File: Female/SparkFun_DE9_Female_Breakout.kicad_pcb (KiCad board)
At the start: 2 copper layers, 22.9 x 31.8 mm, 43 parts, among them J2 Conn_01x09, J3 Conn_01x01, J4 Conn_01x01, J5 DB9-Female

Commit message: Updates symbol, footprint, and design with the new renamed parts
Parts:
- removed J5: DB9-Female, DE9_Footprint:DB9_Female
- added J1: DE9-Female, DE9-Footprints:DE9_Female, F.Cu at (120.3, 108.6)
- moved G*** 0.32 mm to (113.6, 96.5)
- moved Ref** 0.32 mm to (113.6, 121.3)

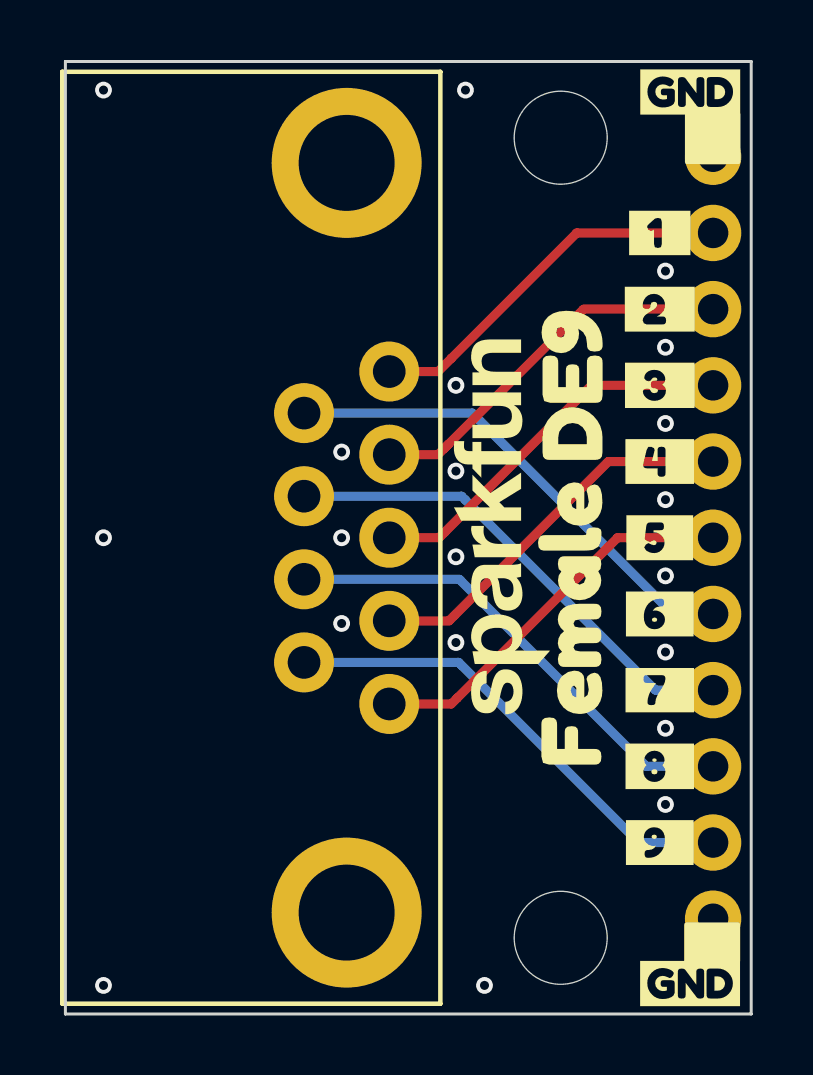
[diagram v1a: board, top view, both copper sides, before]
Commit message: Moves standoff just a bit
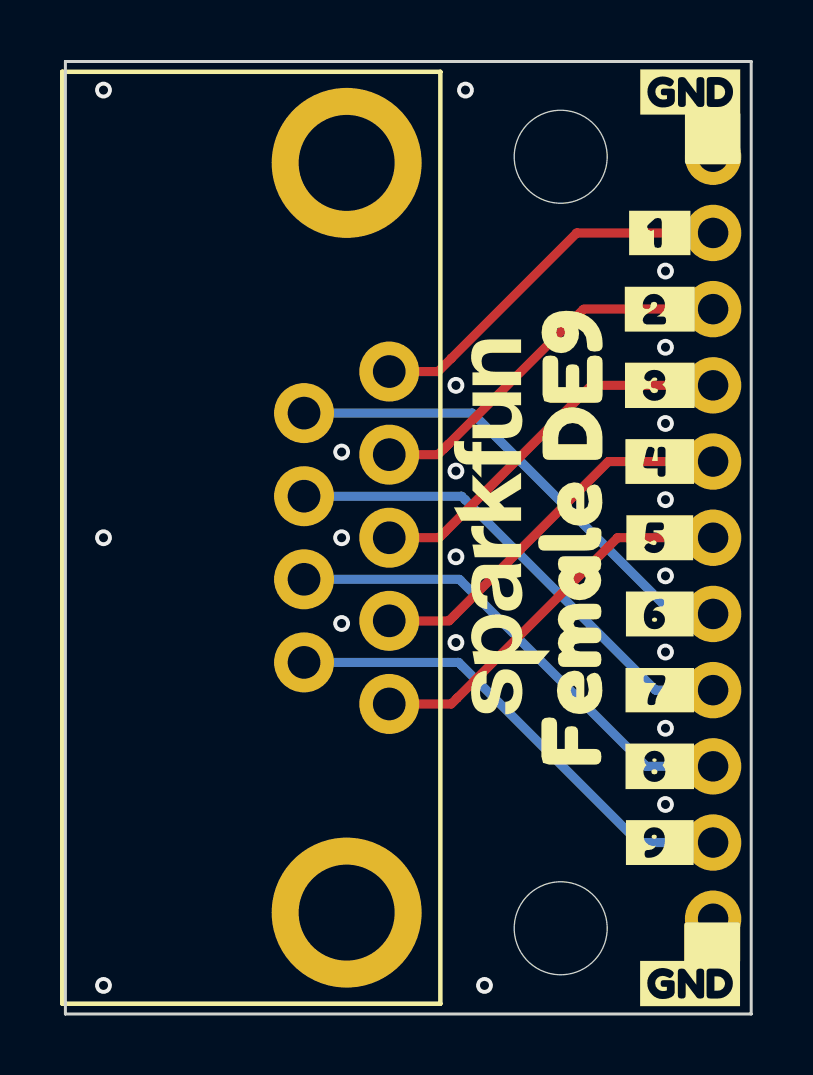
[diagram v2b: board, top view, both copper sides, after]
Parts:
- moved ST1 0.64 mm to (126.0, 95.9)
- moved ST2 0.32 mm to (126.0, 121.6)
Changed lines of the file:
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@@
 	(footprint "SparkFun-Hardware:Standoff"
 		(layer "F.Cu")
-		(at 125.984 95.25)
+		(at 125.984 95.885)
 		(tags "SparkFun")
 		(property "Reference" "ST1"
@@
 	(footprint "SparkFun-Hardware:Standoff"
 		(layer "F.Cu")
-		(at 125.984 121.92)
+		(at 125.984 121.6025)
 		(tags "SparkFun")
 		(property "Reference" "ST2"
@@
 		(layer "Dwgs.User")
 		(pts
-			(xy 132.336 124.46) (xy 132.336 92.71)
+			(xy 125.984 121.6025) (xy 132.334 121.6025)
 		)
-		(height 17.018)
-		(orientation 1)
+		(height 6.35)
+		(orientation 0)
 		(format
 			(prefix "")
@@
 			(keep_text_aligned yes)
 		)
-		(gr_text "1.25 in"
-			(at 148.204 108.585 90)
+		(gr_text "0.25 in"
+			(at 129.159 126.8025 0)
 			(layer "Dwgs.User")
 			(effects
@@
 		(layer "Dwgs.User")
 		(pts
-			(xy 131.064 121.285) (xy 131.064 124.46)
+			(xy 125.984 121.285) (xy 125.984 124.3965)
 		)
-		(height 6.985)
+		(height 12.065)
 		(orientation 1)
 		(format
@@
 			(keep_text_aligned yes)
 		)
-		(gr_text "0.125 in"
-			(at 138.049 115.2525 90)
+		(gr_text "0.1225 in"
+			(at 138.049 114.935 90)
 			(layer "Dwgs.User")
 			(effects
@@
 		(layer "Dwgs.User")
 		(pts
-			(xy 131.064 108.585) (xy 131.064 124.46)
+			(xy 125.984 95.885) (xy 125.984 92.71)
 		)
-		(height 11.43)
+		(height 12.065)
 		(orientation 1)
 		(format
@@
 			(arrow_length 1.27)
 			(text_position_mode 2)
-			(arrow_direction outward)
+			(arrow_direction inward)
 			(extension_height 0.58642)
 			(extension_offset 0.5)
 			(keep_text_aligned yes)
 		)
-		(gr_text "0.625 in"
-			(at 141.344 116.84 90)
+		(gr_text "0.125 in"
+			(at 138.049 101.9175 90)
 			(layer "Dwgs.User")
 			(effects
@@
 		(layer "Dwgs.User")
 		(pts
-			(xy 132.334 124.46) (xy 109.474 124.46)
+			(xy 132.336 124.46) (xy 132.336 92.71)
 		)
-		(height 6.985)
-		(orientation 0)
+		(height 17.018)
+		(orientation 1)
 		(format
 			(prefix "")
@@
 			(keep_text_aligned yes)
 		)
-		(gr_text "0.9 in"
-			(at 120.904 130.295 0)
+		(gr_text "1.25 in"
+			(at 148.204 108.585 90)
 			(layer "Dwgs.User")
 			(effects
@@
 		(layer "Dwgs.User")
 		(pts
-			(xy 125.984 121.92) (xy 125.984 124.46)
+			(xy 131.064 108.585) (xy 131.064 124.46)
 		)
-		(height 8.255)
+		(height 11.43)
 		(orientation 1)
 		(format
@@
 			(arrow_length 1.27)
 			(text_position_mode 2)
-			(arrow_direction inward)
+			(arrow_direction outward)
+			(extension_height 0.58642)
+			(extension_offset 0.5)
+			(keep_text_aligned yes)
+		)
+		(gr_text "0.625 in"
+			(at 141.344 116.84 90)
+			(layer "Dwgs.User")
+			(effects
+				(font
+					(size 1 1)
+					(thickness 0.15)
+				)
+			)
+		)
+	)
+	(dimension
+		(type orthogonal)
+		(layer "Dwgs.User")
+		(pts
+			(xy 132.334 124.46) (xy 109.474 124.46)
+		)
+		(height 6.985)
+		(orientation 0)
+		(format
+			(prefix "")
+			(suffix "")
+			(units 3)
+			(units_format 1)
+			(precision 4)
+			(suppress_zeroes yes)
+		)
+		(style
+			(thickness 0.15)
+			(arrow_length 1.27)
+			(text_position_mode 0)
+			(arrow_direction outward)
 			(extension_height 0.58642)
 			(extension_offset 0.5)
 			(keep_text_aligned yes)
 		)
-		(gr_text "0.1 in"
-			(at 134.239 116.84 90)
+		(gr_text "0.9 in"
+			(at 120.904 130.295 0)
 			(layer "Dwgs.User")
 			(effects

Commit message: Fixes measure at standoff
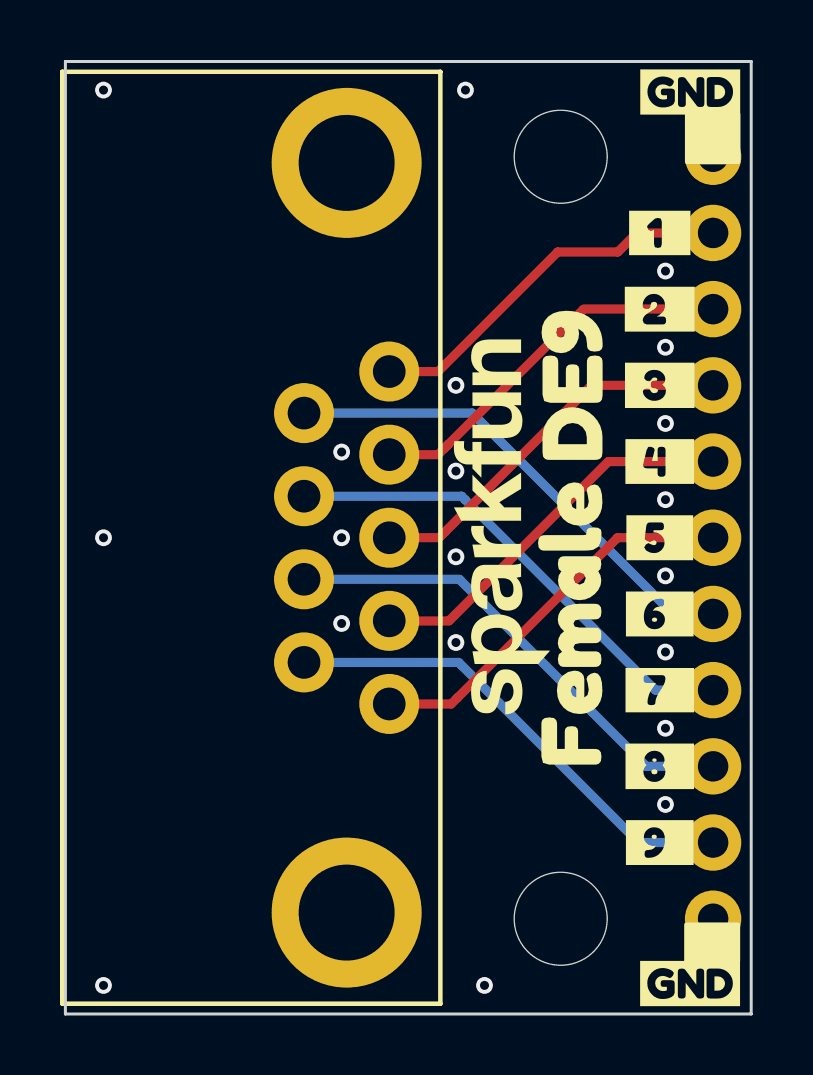
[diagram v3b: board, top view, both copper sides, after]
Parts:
- moved ST2 0.32 mm to (126.0, 121.3)
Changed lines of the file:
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@@
 	(footprint "SparkFun-Hardware:Standoff"
 		(layer "F.Cu")
-		(at 125.984 121.6025)
+		(at 125.984 121.285)
 		(tags "SparkFun")
 		(property "Reference" "ST2"
@@
 		(layer "Dwgs.User")
 		(pts
-			(xy 125.984 121.285) (xy 125.984 124.3965)
+			(xy 125.984 121.285) (xy 125.984 124.46)
 		)
-		(height 12.065)
+		(height 11.7475)
 		(orientation 1)
 		(format
@@
 			(keep_text_aligned yes)
 		)
-		(gr_text "0.1225 in"
-			(at 138.049 114.935 90)
+		(gr_text "0.125 in"
+			(at 137.7315 115.2525 90)
 			(layer "Dwgs.User")
 			(effects
@@
 	)
 	(segment
-		(start 126.5174 98.425)
-		(end 122.33275 102.60965)
+		(start 121.897399 103.045001)
+		(end 125.8824 99.06)
 		(width 0.3048)
 		(layer "F.Cu")
@@
 	)
 	(segment
-		(start 121.897399 103.045001)
-		(end 122.33275 102.60965)
+		(start 120.396 103.045001)
+		(end 121.897399 103.045001)
 		(width 0.3048)
 		(layer "F.Cu")
@@
 	)
 	(segment
-		(start 131.064 98.425)
-		(end 126.5174 98.425)
+		(start 127.889 99.06)
+		(end 128.524 98.425)
 		(width 0.3048)
 		(layer "F.Cu")
@@
 	)
 	(segment
-		(start 120.396 103.045001)
-		(end 121.897399 103.045001)
+		(start 125.8824 99.06)
+		(end 127.889 99.06)
+		(width 0.3048)
+		(layer "F.Cu")
+		(net 3)
+	)
+	(segment
+		(start 128.524 98.425)
+		(end 131.064 98.425)
 		(width 0.3048)
 		(layer "F.Cu")
@@
 		(min_thickness 0.25)
 		(filled_areas_thickness no)
-		(fill yes
+		(fill
 			(thermal_gap 0.5)
 			(thermal_bridge_width 0.5)

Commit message: Updates teh footprints of the DE9 connector to match the symbol
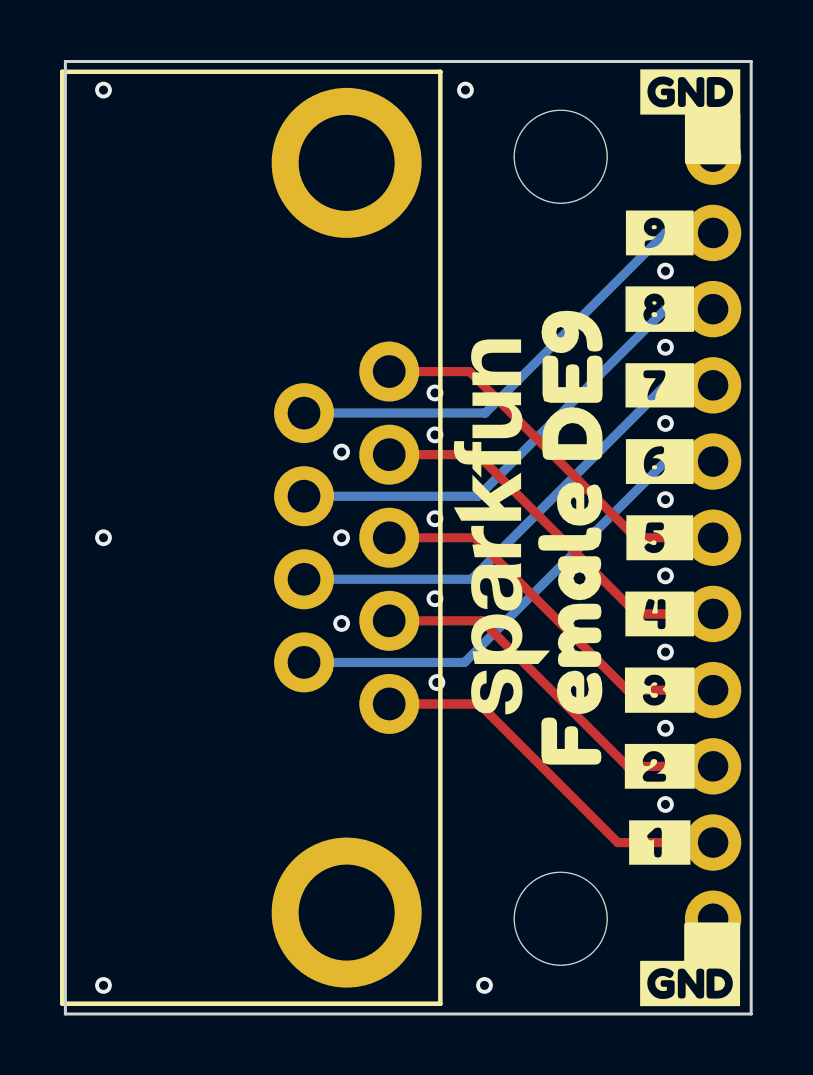
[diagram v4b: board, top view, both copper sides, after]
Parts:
- removed kibuzzard-67DDA384: G***, kibuzzard-67DDA384
- added kibuzzard-67F7FDBF: G***, kibuzzard-67F7FDBF, B.Cu at (129.3, 118.7)
- moved J2 20.3 mm to (131.1, 118.7), turned to 90 degrees
- moved kibuzzard-67D49687 20.3 mm to (129.3, 118.7)
- moved kibuzzard-67D496F6 20.3 mm to (129.3, 98.4)
- moved kibuzzard-67DDA3E0 20.3 mm to (129.3, 98.4)
- moved kibuzzard-67D496B8 15.2 mm to (129.3, 116.2)
- moved kibuzzard-67D496EA 15.2 mm to (129.3, 101.0)
- moved kibuzzard-67DDA391 15.2 mm to (129.3, 116.2)
- moved kibuzzard-67DDA3D5 15.2 mm to (129.3, 101.0)
- moved kibuzzard-67DDBDD7 11.1 mm to (122.5, 103.2)
- moved kibuzzard-67DDBDCA 10.9 mm to (122.6, 114.0)
- moved kibuzzard-67D496C7 10.2 mm to (129.3, 113.7)
- moved kibuzzard-67D496E4 10.2 mm to (129.3, 103.5)
- moved kibuzzard-67DDA399 10.2 mm to (129.3, 113.7)
- moved kibuzzard-67DDA3B8 10.2 mm to (129.3, 103.5)
- moved kibuzzard-67DDBDDC 8.39 mm to (115.5, 104.5)
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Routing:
- net GND: vias 15 -> 16
